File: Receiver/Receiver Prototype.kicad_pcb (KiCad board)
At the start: 4 copper layers, 62 x 40 mm, 39 parts, among them J1 Conn_01x02_Socket, J2 Conn_01x03, J4 Conn_Coaxial, J5 Conn_01x02, J6 Conn_01x02, J7 Conn_Coaxial, J8 Conn_Coaxial, U1 OPA3692ID, U2 AD8692ARZ

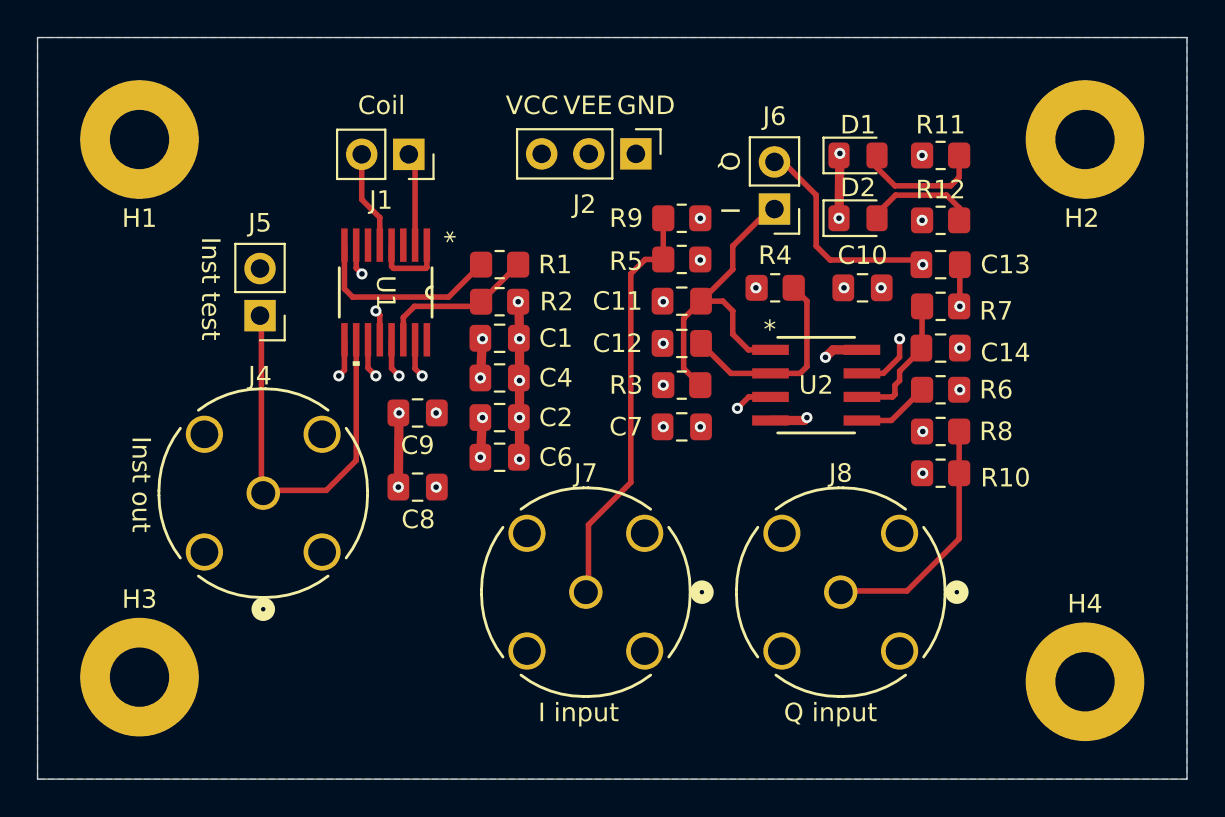
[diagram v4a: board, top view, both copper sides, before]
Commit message: Added models for power regulators and OPA692 buffer. Also added diode clipper schematics
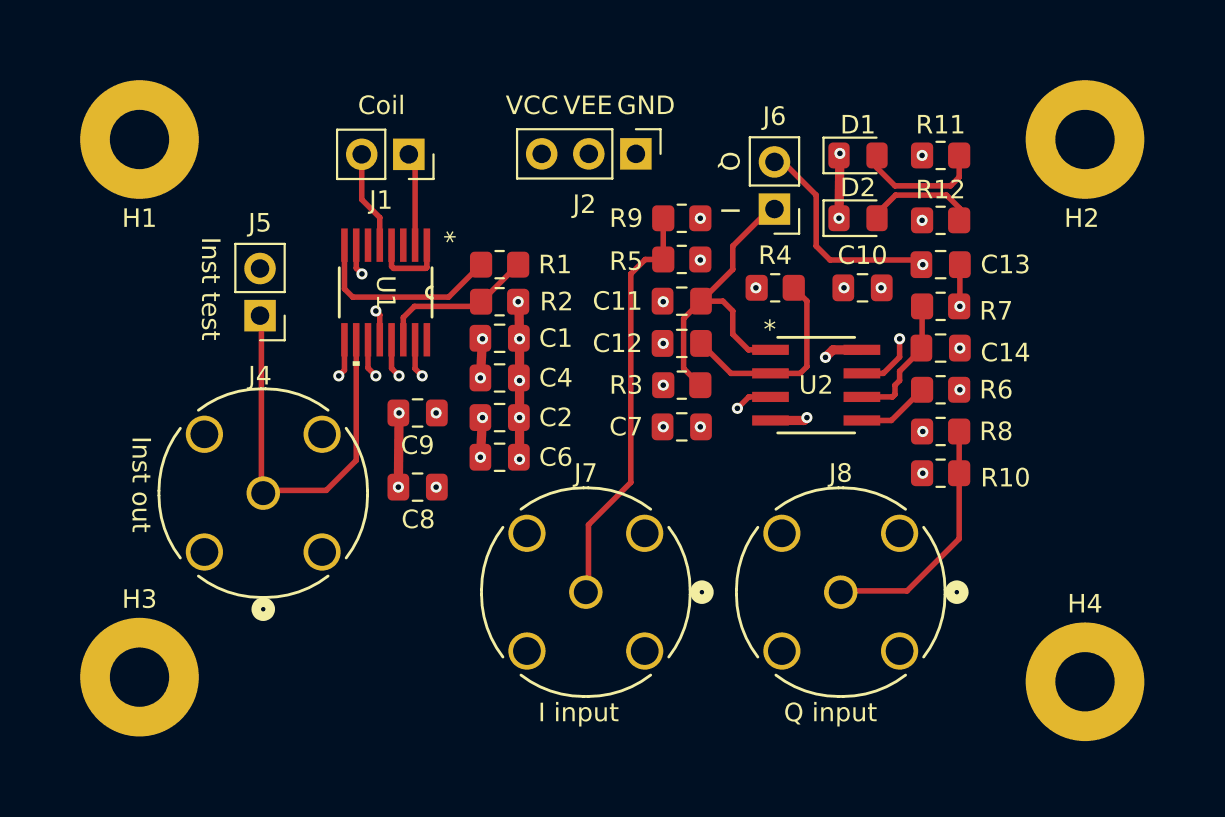
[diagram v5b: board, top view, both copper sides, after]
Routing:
- removed copper zone on In1.Cu, net GND
- removed copper zone on In2.Cu, net VCC
- removed copper zone on B.Cu, net VEE
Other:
- board outline removed
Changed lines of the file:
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@@
 		)
-	)
-	(gr_line
-		(start 138 65)
-		(end 200 65)
-		(stroke
-			(width 0.05)
-			(type default)
-		)
-		(layer "Edge.Cuts")
-	)
-	(gr_line
-		(start 138 105)
-		(end 200 105)
-		(stroke
-			(width 0.05)
-			(type default)
-		)
-		(layer "Edge.Cuts")
-	)
-	(gr_line
-		(start 200 105)
-		(end 200 65)
-		(stroke
-			(width 0.05)
-			(type default)
-		)
-		(layer "Edge.Cuts")
-	)
-	(gr_line
-		(start 138 105)
-		(end 138 65)
-		(stroke
-			(width 0.05)
-			(type default)
-		)
-		(layer "Edge.Cuts")
 	)
 	(gr_text "Receiver 1.0 2024-04-01"
@@
 		)
 	)
-	(dimension
-		(type aligned)
-		(layer "User.1")
-		(pts
-			(xy 138 105) (xy 200 105)
-		)
-		(height 5.25)
-		(gr_text "62,0000 mm"
-			(at 169 109.1 0)
-			(layer "User.1")
-			(effects
-				(font
-					(size 1 1)
-					(thickness 0.15)
-				)
-			)
-		)
-		(format
-			(prefix "")
-			(suffix "")
-			(units 3)
-			(units_format 1)
-			(precision 4)
-		)
-		(style
-			(thickness 0.1)
-			(arrow_length 1.27)
-			(text_position_mode 0)
-			(extension_height 0.58642)
-			(extension_offset 0.5) keep_text_aligned)
-	)
-	(dimension
-		(type aligned)
-		(layer "User.1")
-		(pts
-			(xy 200 65) (xy 200 105)
-		)
-		(height -15.75)
-		(gr_text "40,0000 mm"
-			(at 214.6 85 90)
-			(layer "User.1")
-			(effects
-				(font
-					(size 1 1)
-					(thickness 0.15)
-				)
-			)
-		)
-		(format
-			(prefix "")
-			(suffix "")
-			(units 3)
-			(units_format 1)
-			(precision 4)
-		)
-		(style
-			(thickness 0.1)
-			(arrow_length 1.27)
-			(text_position_mode 0)
-			(extension_height 0.58642)
-			(extension_offset 0.5) keep_text_aligned)
-	)
 	(segment
 		(start 164 83.5)
@@
 		(net 25)
 	)
-	(zone
-		(net 1)
-		(net_name "GND")
-		(layer "In1.Cu")
-		(hatch edge 0.5)
-		(connect_pads
-			(clearance 0.5)
-		)
-		(min_thickness 0.25)
-		(filled_areas_thickness no)
-		(fill yes
-			(thermal_gap 0.5)
-			(thermal_bridge_width 0.5)
-		)
-		(polygon
-			(pts
-				(xy 138 65) (xy 200 65) (xy 200 105) (xy 138 105)
-			)
-		)
-	)
-	(zone
-		(net 2)
-		(net_name "VCC")
-		(layer "In2.Cu")
-		(hatch edge 0.5)
-		(priority 1)
-		(connect_pads
-			(clearance 0.5)
-		)
-		(min_thickness 0.25)
-		(filled_areas_thickness no)
-		(fill yes
-			(thermal_gap 0.5)
-			(thermal_bridge_width 0.5)
-		)
-		(polygon
-			(pts
-				(xy 138 65) (xy 200 65) (xy 200 105) (xy 138 105)
-			)
-		)
-	)
-	(zone
-		(net 3)
-		(net_name "VEE")
-		(layer "B.Cu")
-		(hatch edge 0.5)
-		(priority 2)
-		(connect_pads
-			(clearance 0.5)
-		)
-		(min_thickness 0.25)
-		(filled_areas_thickness no)
-		(fill yes
-			(thermal_gap 0.5)
-			(thermal_bridge_width 0.5)
-		)
-		(polygon
-			(pts
-				(xy 138 65) (xy 200 65) (xy 200 105) (xy 138 105)
-			)
-		)
-	)
 )

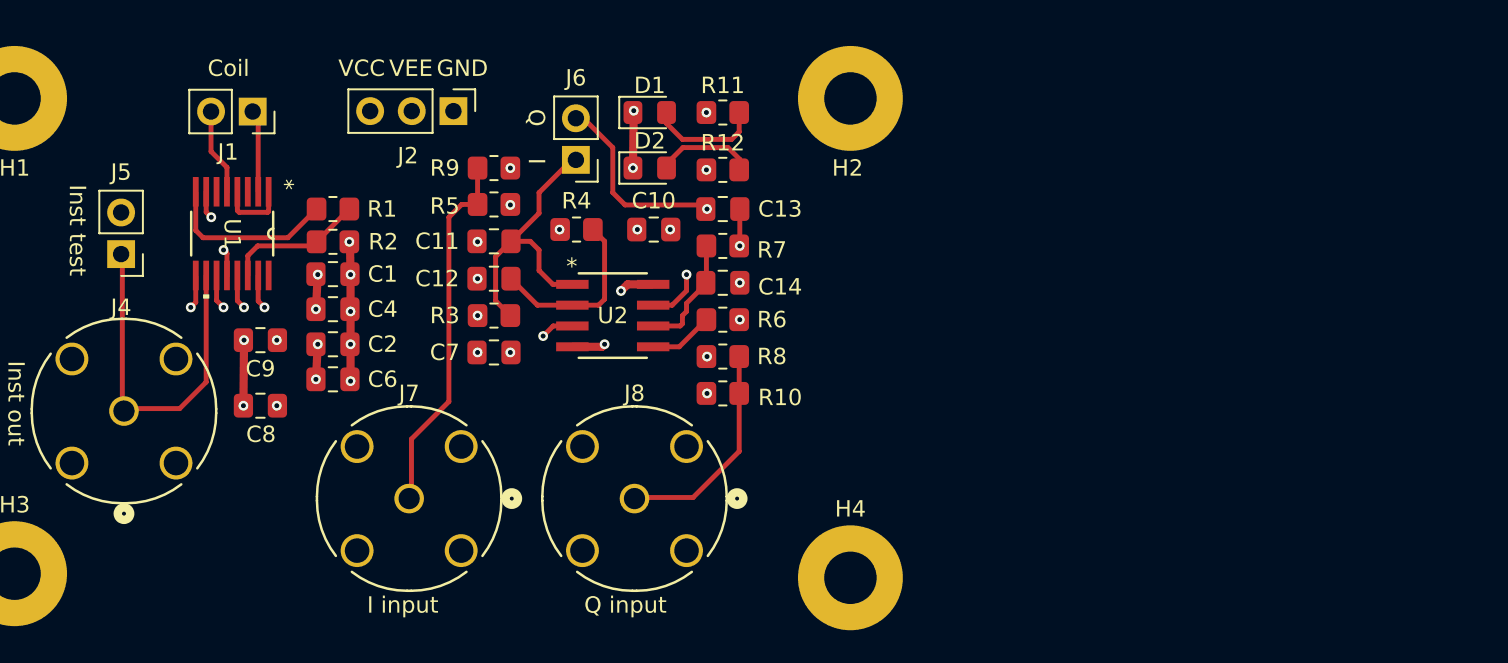
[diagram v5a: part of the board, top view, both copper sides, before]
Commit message: Added AD607 to schematic
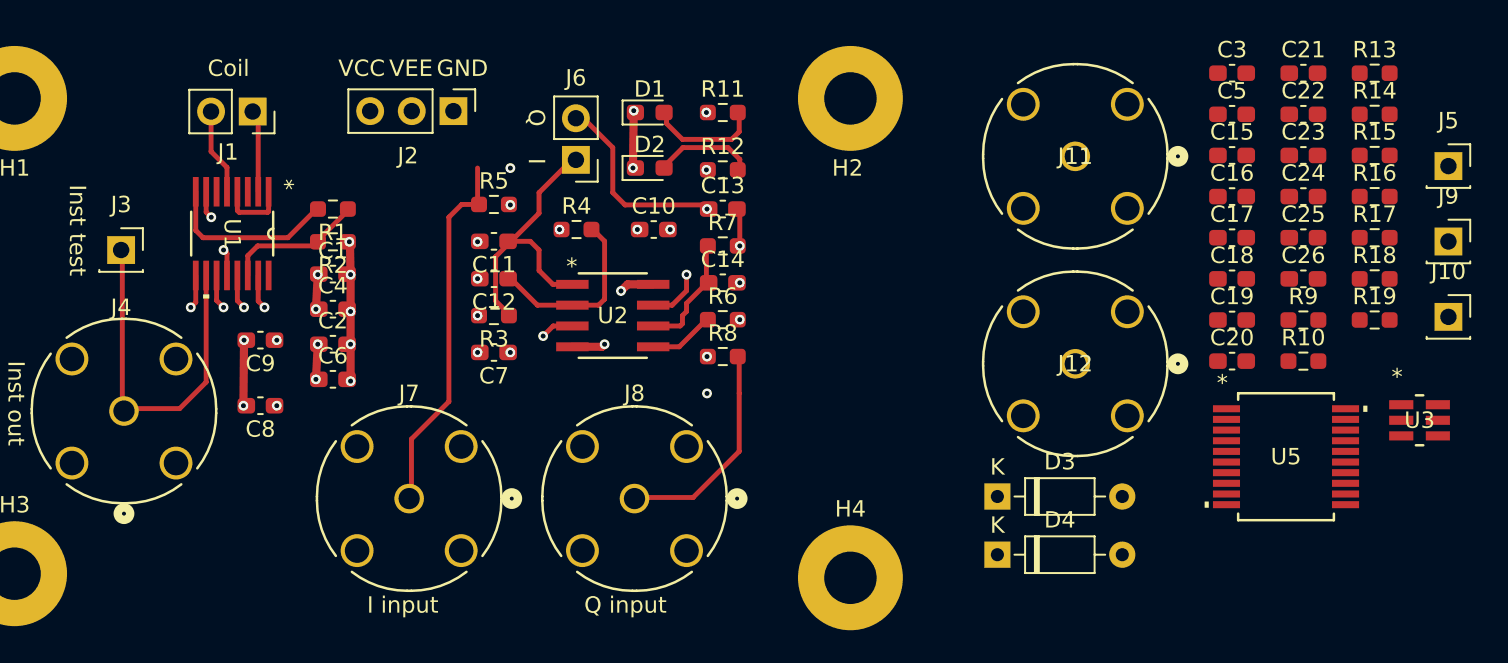
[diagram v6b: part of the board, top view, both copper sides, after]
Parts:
- added C15: 4 nF, Capacitor_SMD:C_0603_1608Metric_Pad1.08x0.95mm_HandSolder, F.Cu at (217.8, 74.0)
- added C16: 10n, Capacitor_SMD:C_0603_1608Metric_Pad1.08x0.95mm_HandSolder, F.Cu at (217.8, 76.5)
- added C17: 0.1u, Capacitor_SMD:C_0603_1608Metric_Pad1.08x0.95mm_HandSolder, F.Cu at (217.8, 79.0)
- added C18: 1n, Capacitor_SMD:C_0603_1608Metric_Pad1.08x0.95mm_HandSolder, F.Cu at (217.8, 81.5)
- added C19: 0.1u, Capacitor_SMD:C_0603_1608Metric_Pad1.08x0.95mm_HandSolder, F.Cu at (217.8, 84.0)
- added C20: 0.1u, Capacitor_SMD:C_0603_1608Metric_Pad1.08x0.95mm_HandSolder, F.Cu at (217.8, 86.5)
- added C21: 0.1u, Capacitor_SMD:C_0603_1608Metric_Pad1.08x0.95mm_HandSolder, F.Cu at (222.1, 69.0)
- added C22: 10n, Capacitor_SMD:C_0603_1608Metric_Pad1.08x0.95mm_HandSolder, F.Cu at (222.1, 71.5)
- added C23: 0.1u, Capacitor_SMD:C_0603_1608Metric_Pad1.08x0.95mm_HandSolder, F.Cu at (222.1, 74.0)
- added C24: 0.1u, Capacitor_SMD:C_0603_1608Metric_Pad1.08x0.95mm_HandSolder, F.Cu at (222.1, 76.5)
- added C25: 47p, Capacitor_SMD:C_0603_1608Metric_Pad1.08x0.95mm_HandSolder, F.Cu at (222.1, 79.0)
- added C26: 1n, Capacitor_SMD:C_0603_1608Metric_Pad1.08x0.95mm_HandSolder, F.Cu at (222.1, 81.5)
- added C3: 0.1u, Capacitor_SMD:C_0603_1608Metric_Pad1.08x0.95mm_HandSolder, F.Cu at (217.8, 69.0)
- added C5: 0.1u, Capacitor_SMD:C_0603_1608Metric_Pad1.08x0.95mm_HandSolder, F.Cu at (217.8, 71.5)
- added D3: 1N4148, Diode_THT:D_DO-35_SOD27_P7.62mm_Horizontal, F.Cu at (203.5, 94.8)
- added D4: 1N4148, Diode_THT:D_DO-35_SOD27_P7.62mm_Horizontal, F.Cu at (203.5, 98.3)
- added J10: Conn_01x01, Connector_PinSocket_2.54mm:PinSocket_1x01_P2.54mm_Vertical, F.Cu at (231.0, 83.8)
- added J11: Conn_Coaxial, BNC 112404:CONN_112404_AMP, F.Cu at (208.2, 74.0)
- added J12: Conn_Coaxial, BNC 112404:CONN_112404_AMP, F.Cu at (208.2, 86.7)
- added J3: Conn_01x01, Connector_PinSocket_2.54mm:PinSocket_1x01_P2.54mm_Vertical, F.Cu at (150.0, 79.8)
- added J9: Conn_01x01, Connector_PinSocket_2.54mm:PinSocket_1x01_P2.54mm_Vertical, F.Cu at (231.0, 79.2)
- added R13: R, Resistor_SMD:R_0603_1608Metric_Pad0.98x0.95mm_HandSolder, F.Cu at (226.5, 69.0)
- added R14: R, Resistor_SMD:R_0603_1608Metric_Pad0.98x0.95mm_HandSolder, F.Cu at (226.5, 71.5)
- added R15: 51.1, Resistor_SMD:R_0603_1608Metric_Pad0.98x0.95mm_HandSolder, F.Cu at (226.5, 74.0)
- added R16: 4.99k, Resistor_SMD:R_0603_1608Metric_Pad0.98x0.95mm_HandSolder, F.Cu at (226.5, 76.5)
- added R17: OPEN, Resistor_SMD:R_0603_1608Metric_Pad0.98x0.95mm_HandSolder, F.Cu at (226.5, 79.0)
- added R18: 332, Resistor_SMD:R_0603_1608Metric_Pad0.98x0.95mm_HandSolder, F.Cu at (226.5, 81.5)
- added R19: 316, Resistor_SMD:R_0603_1608Metric_Pad0.98x0.95mm_HandSolder, F.Cu at (226.5, 84.0)
- added U3: OPA692IDBVR, OPA692 SOT-23:DBV6, F.Cu at (229.2, 90.1)
- added U5: AD607ARSZ, AD607ARSZ:RS_20_ADI, F.Cu at (221.1, 92.4)
- C1, C10, C11, C12, C13, C14, C2, C4, C6, C7, C8, C9: footprint Capacitor_SMD:C_0805_2012Metric_Pad1.18x1.45mm_HandSolder -> Capacitor_SMD:C_0603_1608Metric_Pad1.08x0.95mm_HandSolder
- D1, D2: footprint LED_SMD:LED_0805_2012Metric_Pad1.15x1.40mm_HandSolder -> LED_SMD:LED_0603_1608Metric_Pad1.05x0.95mm_HandSolder
- J5: value Conn_01x02 -> Conn_01x01; footprint Connector_PinHeader_2.54mm:PinHeader_1x02_P2.54mm_Vertical -> Connector_PinSocket_2.54mm:PinSocket_1x01_P2.54mm_Vertical
- R1, R11, R12, R2, R3, R4, R5, R6, R7, R8: footprint Resistor_SMD:R_0805_2012Metric_Pad1.20x1.40mm_HandSolder -> Resistor_SMD:R_0603_1608Metric_Pad0.98x0.95mm_HandSolder
- R10: value 50 -> R; footprint Resistor_SMD:R_0805_2012Metric_Pad1.20x1.40mm_HandSolder -> Resistor_SMD:R_0603_1608Metric_Pad0.98x0.95mm_HandSolder
- R9: value 50 -> 50 Ohm; footprint Resistor_SMD:R_0805_2012Metric_Pad1.20x1.40mm_HandSolder -> Resistor_SMD:R_0603_1608Metric_Pad0.98x0.95mm_HandSolder
- moved J5 81.2 mm to (231.0, 74.6), turned to 0 degrees
- moved R9 50.2 mm to (222.1, 84.0), turned to 0 degrees
- moved R10 35.5 mm to (222.1, 86.5)
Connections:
- J4 pad 3: GND -> (no net)
- J4 pad 4: GND -> (no net)
- J4 pad 5: GND -> (no net)
- J5 pad 1: /Inst_Out -> GND
- J7 pad 3: GND -> (no net)
- J7 pad 4: GND -> (no net)
- J7 pad 5: GND -> (no net)
- J8 pad 3: GND -> (no net)
- J8 pad 4: GND -> (no net)
- J8 pad 5: GND -> (no net)
- R10 pad 1: GND -> Net-(U3-OUPUT)
- R10 pad 2: /Q_Filter_In -> Net-(D3-K)
- R9 pad 1: GND -> Net-(U3-IN+)
- R9 pad 2: /I_Filter_In -> GND
